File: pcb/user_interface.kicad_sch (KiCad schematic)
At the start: 18 parts, among them Q6 NTR4003N, SW4 GSPTS0018, SW5 GSPTS0018, SW6 GSPTS0018, SW7 GSPTS0018

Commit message: Add MPN field for components except resistors
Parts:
- BZ1: MPN (none) -> CEM-1203(42)
- D3, D5: MPN (none) -> B38G3RGB-10D0003H2U1930
- D4: MPN (none) -> SS12
- Q6: MPN (none) -> NTR4003N
- S1: MPN (none) -> RDS4-8S-1012-73-RA-254-D-67
- SW4, SW5, SW6, SW7: MPN (none) -> GSPTS0018
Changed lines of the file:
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@@
+			)
+		)
+		(property "MPN" "CEM-1203(42)"
+			(at 66.04 133.35 0)
+			(effects
+				(font
+					(size 1.27 1.27)
+				)
+				(hide yes)
 			)
 		)
@@
 		)
 		(property "Description" "Resistor, small US symbol"
+			(at 50.8 45.72 0)
+			(effects
+				(font
+					(size 1.27 1.27)
+				)
+				(hide yes)
+			)
+		)
+		(property "MPN" ""
 			(at 50.8 45.72 0)
 			(effects
@@
 			)
 		)
+		(property "MPN" "GSPTS0018"
+			(at 101.6 88.9 90)
+			(effects
+				(font
+					(size 1.27 1.27)
+				)
+				(hide yes)
+			)
+		)
 		(pin "2"
 		)
@@
 			)
 		)
+		(property "MPN" "SS12"
+			(at 60.96 133.35 90)
+			(effects
+				(font
+					(size 1.27 1.27)
+				)
+				(hide yes)
+			)
+		)
 		(pin "2"
 		)
@@
 			)
 		)
+		(property "MPN" ""
+			(at 50.8 158.75 0)
+			(effects
+				(font
+					(size 1.27 1.27)
+				)
+				(hide yes)
+			)
+		)
 		(pin "2"
 		)
@@
 			)
 		)
+		(property "MPN" "B38G3RGB-10D0003H2U1930"
+			(at 50.8 33.02 90)
+			(effects
+				(font
+					(size 1.27 1.27)
+				)
+				(hide yes)
+			)
+		)
 		(pin "1"
 		)
@@
 			)
 		)
+		(property "MPN" "GSPTS0018"
+			(at 158.75 88.9 90)
+			(effects
+				(font
+					(size 1.27 1.27)
+				)
+				(hide yes)
+			)
+		)
 		(pin "2"
 		)
@@
 		)
 		(property "Description" "Resistor, small US symbol"
+			(at 127 45.72 0)
+			(effects
+				(font
+					(size 1.27 1.27)
+				)
+				(hide yes)
+			)
+		)
+		(property "MPN" ""
 			(at 127 45.72 0)
 			(effects
@@
 			)
 		)
+		(property "MPN" ""
+			(at 114.3 45.72 0)
+			(effects
+				(font
+					(size 1.27 1.27)
+				)
+				(hide yes)
+			)
+		)
 		(pin "1"
 		)
@@
 		)
 		(property "Description" "Resistor, small US symbol"
+			(at 139.7 45.72 0)
+			(effects
+				(font
+					(size 1.27 1.27)
+				)
+				(hide yes)
+			)
+		)
+		(property "MPN" ""
 			(at 139.7 45.72 0)
 			(effects
@@
 			)
 		)
+		(property "MPN" "B38G3RGB-10D0003H2U1930"
+			(at 127 33.02 90)
+			(effects
+				(font
+					(size 1.27 1.27)
+				)
+				(hide yes)
+			)
+		)
 		(pin "1"
 		)
@@
 		(property "Description" "8 Position, Through Hole, 2.54 mm Pitch, IP67, Right Angle, 7.3 mm Raised Actuator, DIP Switch"
 			(at 49.53 79.248 0)
+			(effects
+				(font
+					(size 1.27 1.27)
+				)
+				(hide yes)
+			)
+		)
+		(property "MPN" "RDS4-8S-1012-73-RA-254-D-67"
+			(at 50.8 85.09 0)
 			(effects
 				(font
@@
 			)
 		)
+		(property "MPN" "GSPTS0018"
+			(at 139.7 88.9 90)
+			(effects
+				(font
+					(size 1.27 1.27)
+				)
+				(hide yes)
+			)
+		)
 		(pin "2"
 		)
@@
 			)
 		)
+		(property "MPN" "GSPTS0018"
+			(at 120.65 88.9 90)
+			(effects
+				(font
+					(size 1.27 1.27)
+				)
+				(hide yes)
+			)
+		)
 		(pin "2"
 		)
@@
 			)
 		)
+		(property "MPN" ""
+			(at 44.45 152.4 90)
+			(effects
+				(font
+					(size 1.27 1.27)
+				)
+				(hide yes)
+			)
+		)
 		(pin "2"
 		)
@@
 			)
 		)
+		(property "MPN" "NTR4003N"
+			(at 60.96 152.4 0)
+			(effects
+				(font
+					(size 1.27 1.27)
+				)
+				(hide yes)
+			)
+		)
 		(pin "3"
 		)
@@
 			)
 		)
+		(property "MPN" ""
+			(at 38.1 45.72 0)
+			(effects
+				(font
+					(size 1.27 1.27)
+				)
+				(hide yes)
+			)
+		)
 		(pin "1"
 		)
@@
 			(at 63.5 45.72 0)
 			(effects
+				(font
+					(size 1.27 1.27)
+				)
+				(hide yes)
+			)
+		)
+		(property "MPN" ""
+			(at 63.5 45.72 0)
+			(effects

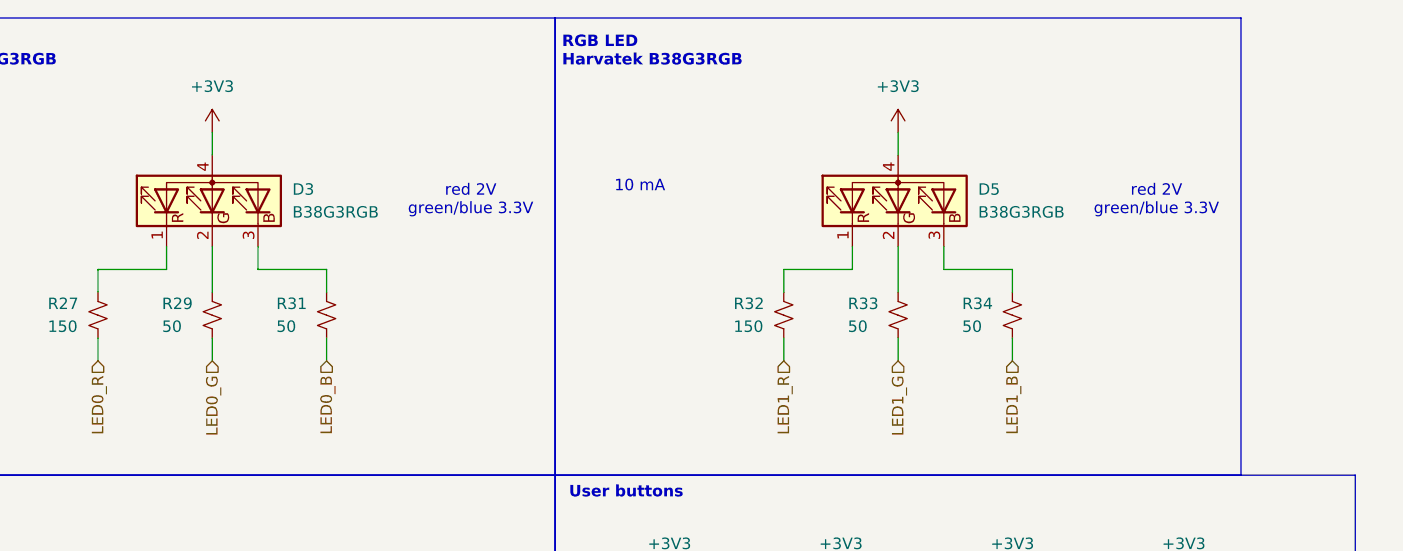
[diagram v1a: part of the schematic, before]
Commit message: BOM optimize RGB LED resistors
50 ohm current limiting resistors on G/B channels -> 47 ohm to match MCU VREF+
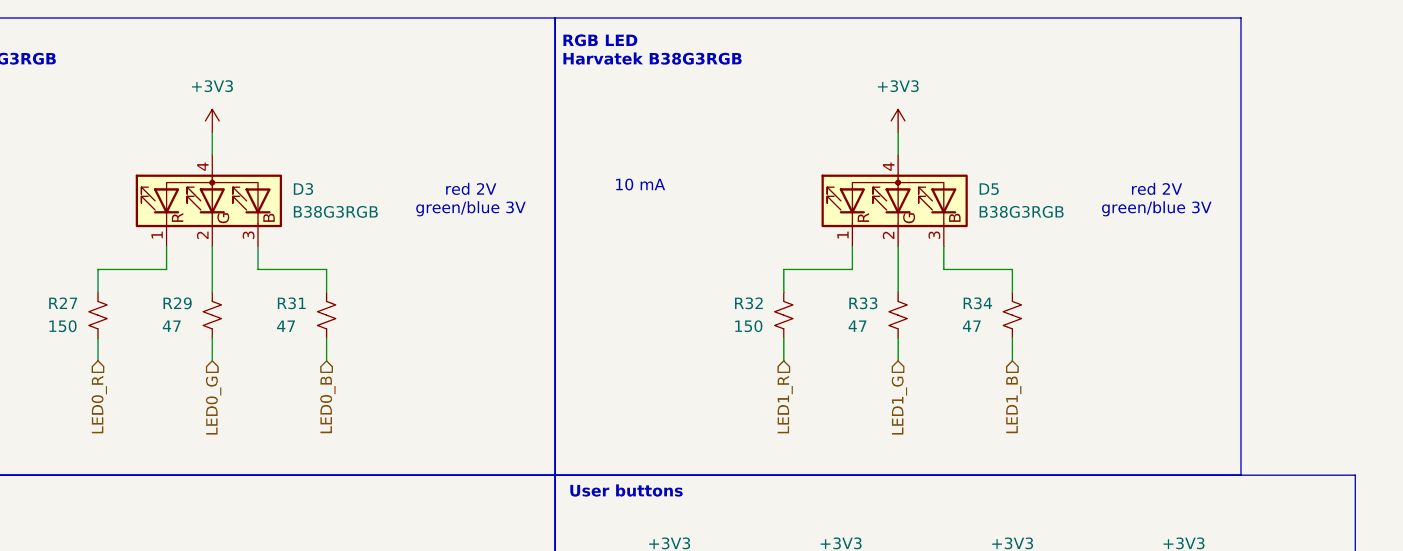
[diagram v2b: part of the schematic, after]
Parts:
- R29, R31, R33, R34: value 50 -> 47
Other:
- note added: "red 2V green/blue 3V"
- note removed: "red 2V green/blue 3.3V"
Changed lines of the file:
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@@
 		)
 	)
-	(text "red 2V\ngreen/blue 3.3V"
+	(text "red 2V\ngreen/blue 3V"
 		(exclude_from_sim no)
 		(at 79.502 33.02 0)
@@
 		)
 	)
-	(text "red 2V\ngreen/blue 3.3V"
+	(text "red 2V\ngreen/blue 3V"
 		(exclude_from_sim no)
 		(at 155.702 33.02 0)
@@
 			)
 		)
-		(property "Value" "50"
+		(property "Value" "47"
 			(at 45.212 46.99 0)
 			(effects
@@
 			)
 		)
-		(property "Value" "50"
+		(property "Value" "47"
 			(at 121.412 46.99 0)
 			(effects
@@
 			)
 		)
-		(property "Value" "50"
+		(property "Value" "47"
 			(at 134.112 46.99 0)
 			(effects
@@
 			)
 		)
-		(property "Value" "50"
+		(property "Value" "47"
 			(at 57.912 46.99 0)
 			(effects

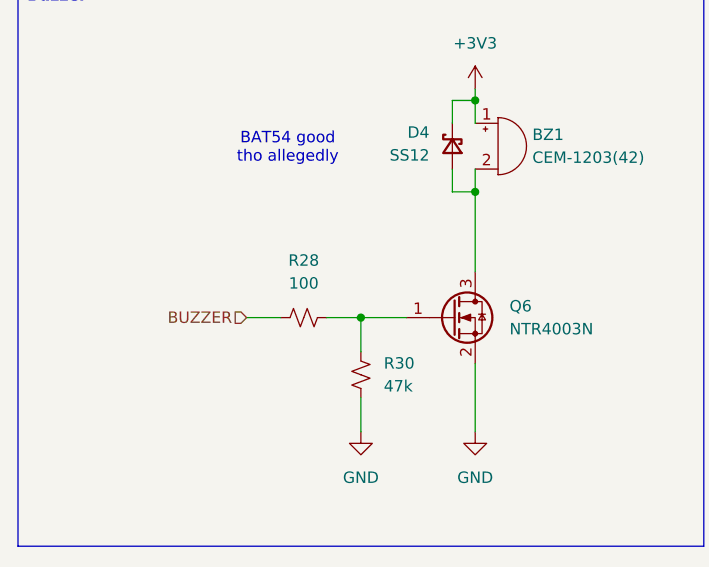
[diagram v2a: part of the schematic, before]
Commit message: BOM optimize 100 ohm resistors to 150 ohm
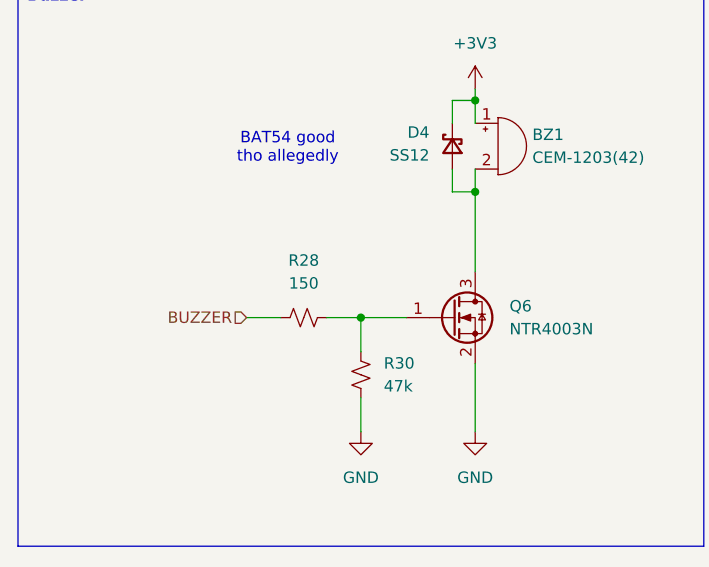
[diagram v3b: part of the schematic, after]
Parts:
- R28: value 100 -> 150
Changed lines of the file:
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@@
 			)
 		)
-		(property "Value" "100"
+		(property "Value" "150"
 			(at 44.45 148.59 90)
 			(effects

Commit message: Update resistor MPNs
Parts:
- R27, R28, R32: MPN (none) -> RC0603JR-07150RL
- R29, R31, R33, R34: MPN (none) -> RC0603JR-1347RL
- R30: MPN (none) -> RC0603FR-0747KL
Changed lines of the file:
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@@
 			)
 		)
-		(property "MPN" ""
+		(property "MPN" "RC0603JR-1347RL"
 			(at 50.8 45.72 0)
 			(effects
@@
 			)
 		)
-		(property "MPN" ""
+		(property "MPN" "RC0603FR-0747KL"
 			(at 50.8 158.75 0)
 			(effects
@@
 			)
 		)
-		(property "MPN" ""
+		(property "MPN" "RC0603JR-1347RL"
 			(at 127 45.72 0)
 			(effects
@@
 			)
 		)
-		(property "MPN" ""
+		(property "MPN" "RC0603JR-07150RL"
 			(at 114.3 45.72 0)
 			(effects
@@
 			)
 		)
-		(property "MPN" ""
+		(property "MPN" "RC0603JR-1347RL"
 			(at 139.7 45.72 0)
 			(effects
@@
 			)
 		)
-		(property "MPN" ""
+		(property "MPN" "RC0603JR-07150RL"
 			(at 44.45 152.4 90)
 			(effects
@@
 			)
 		)
-		(property "MPN" ""
+		(property "MPN" "RC0603JR-07150RL"
 			(at 38.1 45.72 0)
 			(effects
@@
 			)
 		)
-		(property "MPN" ""
+		(property "MPN" "RC0603JR-1347RL"
 			(at 63.5 45.72 0)
 			(effects

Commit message: Update MPNs to optimize for HQ Online
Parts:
- R29, R31, R33, R34: MPN RC0603JR-1347RL -> RC0603FR-0747RL
- SW4, SW5, SW6, SW7: MPN GSPTS0018 -> SKRPADE010
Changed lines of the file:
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@@
 			)
 		)
-		(property "MPN" "RC0603JR-1347RL"
+		(property "MPN" "RC0603FR-0747RL"
 			(at 50.8 45.72 0)
 			(effects
@@
 			)
 		)
-		(property "MPN" "GSPTS0018"
+		(property "MPN" "SKRPADE010"
 			(at 101.6 88.9 90)
 			(effects
@@
 			)
 		)
-		(property "MPN" "GSPTS0018"
+		(property "MPN" "SKRPADE010"
 			(at 158.75 88.9 90)
 			(effects
@@
 			)
 		)
-		(property "MPN" "RC0603JR-1347RL"
+		(property "MPN" "RC0603FR-0747RL"
 			(at 127 45.72 0)
 			(effects
@@
 			)
 		)
-		(property "MPN" "RC0603JR-1347RL"
+		(property "MPN" "RC0603FR-0747RL"
 			(at 139.7 45.72 0)
 			(effects
@@
 			)
 		)
-		(property "MPN" "GSPTS0018"
+		(property "MPN" "SKRPADE010"
 			(at 139.7 88.9 90)
 			(effects
@@
 			)
 		)
-		(property "MPN" "GSPTS0018"
+		(property "MPN" "SKRPADE010"
 			(at 120.65 88.9 90)
 			(effects
@@
 			)
 		)
-		(property "MPN" "RC0603JR-1347RL"
+		(property "MPN" "RC0603FR-0747RL"
 			(at 63.5 45.72 0)
 			(effects

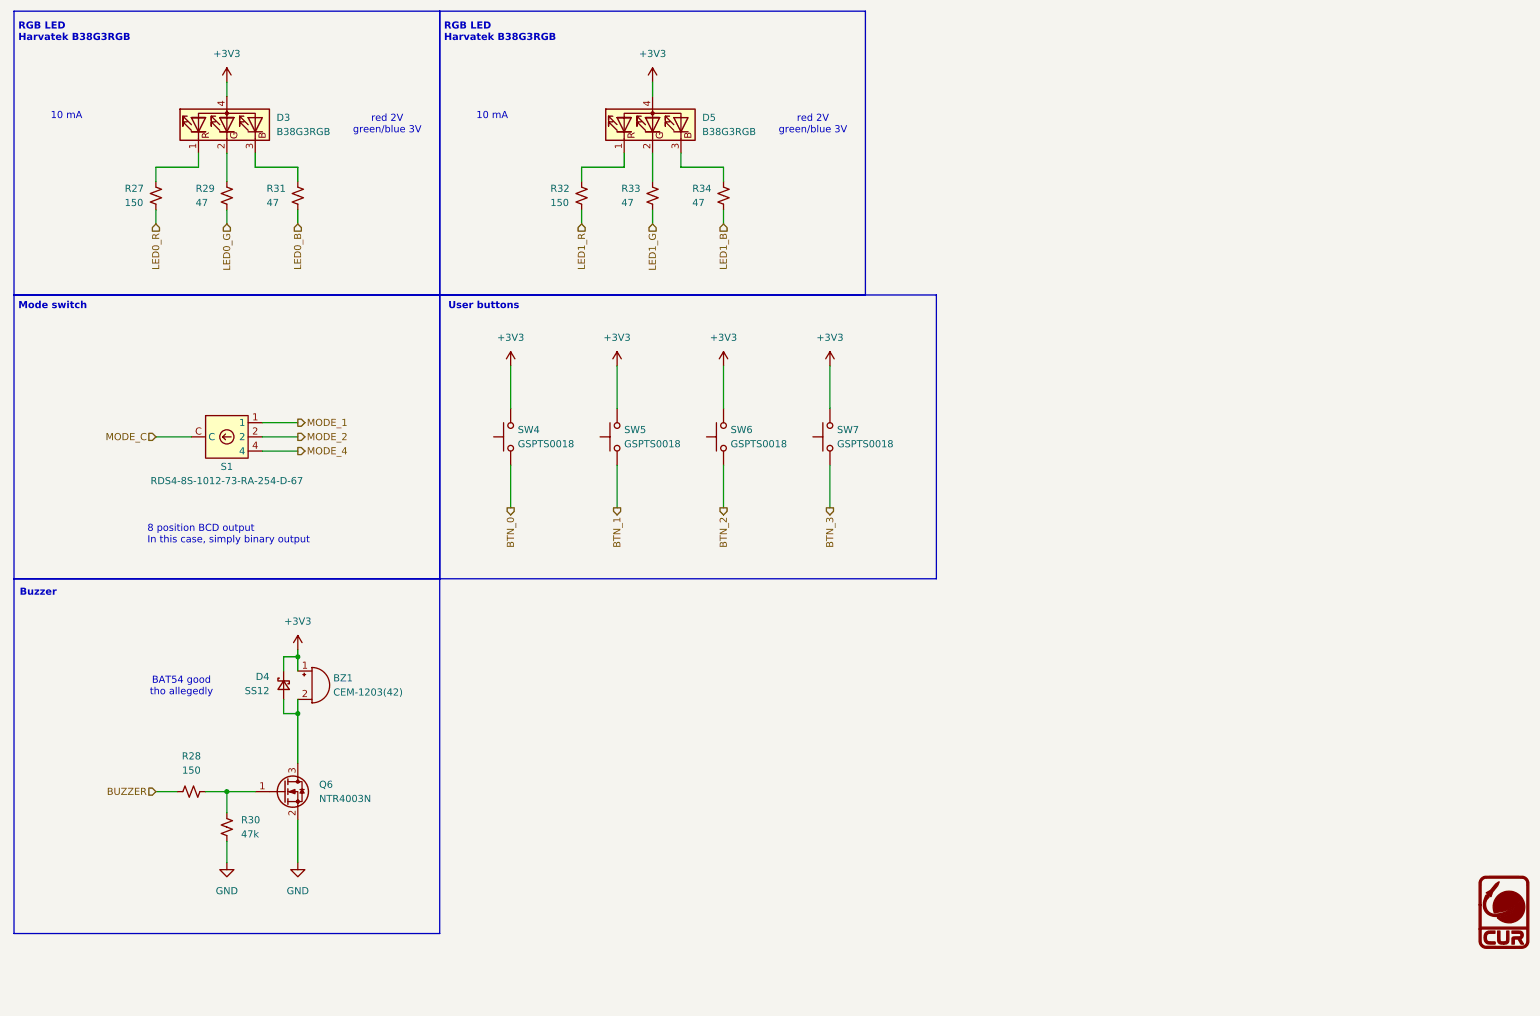
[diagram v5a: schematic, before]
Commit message: Replace RGB LED symbol in user interface schematic
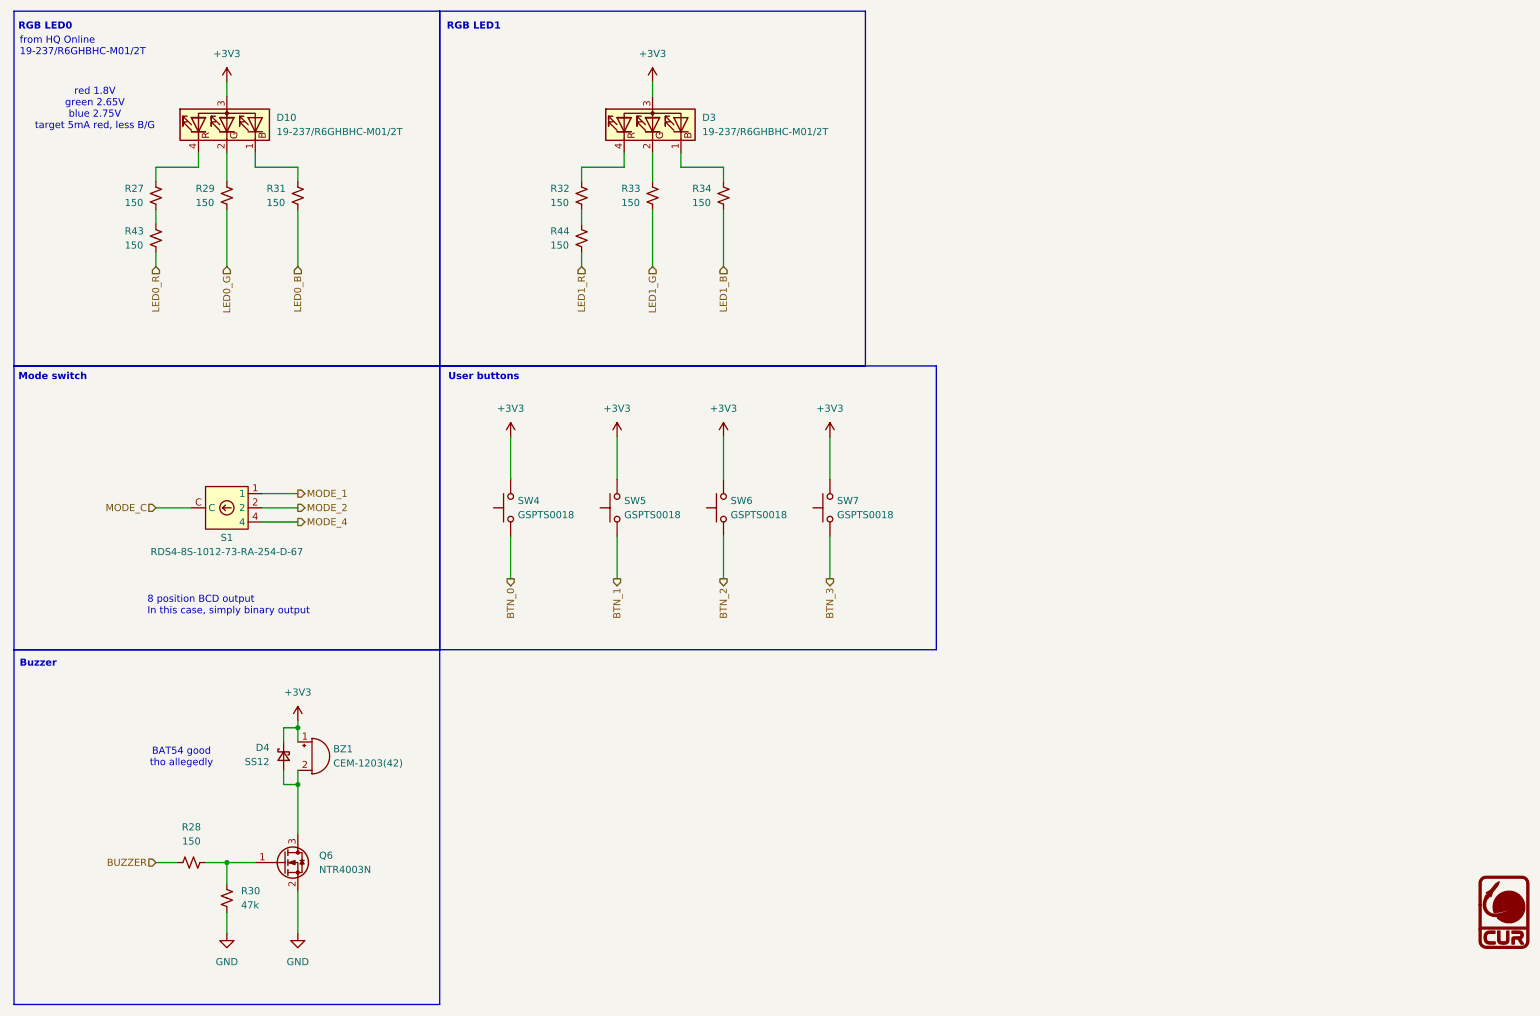
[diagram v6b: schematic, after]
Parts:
- removed D3, D5: B38G3RGB, B38G3RGB:B38G3RGB-10D0003H2U1930_HVK, symbol Device:LED_RGBA
- added D10, D3: 19-237/R6GHBHC-M01/2T, LED_Everlight:19-237R6GHBHC-M012T, symbol Device:LED_BGAR
- added R43, R44: 150, Resistor_SMD:R_0603_1608Metric, symbol Device:R_Small_US
- R29, R31, R33, R34: value 47 -> 150
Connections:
- net +3V3: now also D10.3 (A), D3.3 (A)
- net LED0_R: now also R43.2; no longer R27.2
- net LED1_R: now also R44.2; no longer R32.2
- net at R29.1: now also D10.2 (GK)
- net at R27.1: now also D10.4 (RK)
- net at R31.1: now also D10.1 (BK)
- net at R33.1: now also D3.2 (GK)
- net at R32.1: now also D3.4 (RK)
- net at R34.1: now also D3.1 (BK)
- new net: R32.2, R44.1
- new net: R27.2, R43.1
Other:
- note added: "RGB LED0"
- note added: "RGB LED1"
- note added: "from HQ Online 19-237/R6GHBHC-M01/2T"
- note added: "red 1.8V green 2.65V blue 2.75V target 5mA red, less B/G"
- note removed: "10 mA"
- note removed: "RGB LED Harvatek B38G3RGB"
- note removed: "red 2V green/blue 3V"
- moved on the sheet: BZ1, D4, Q6, R28, R30, S1, SW4, SW5, SW6, SW7
